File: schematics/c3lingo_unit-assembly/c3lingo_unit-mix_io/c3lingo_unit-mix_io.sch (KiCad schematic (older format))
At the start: 34 parts, among them J3 Stage Line-In, J4 Mix Line-Out, J6 PowerSupply, U3 LM833N, U4 DRV134PA, U5 LM833N

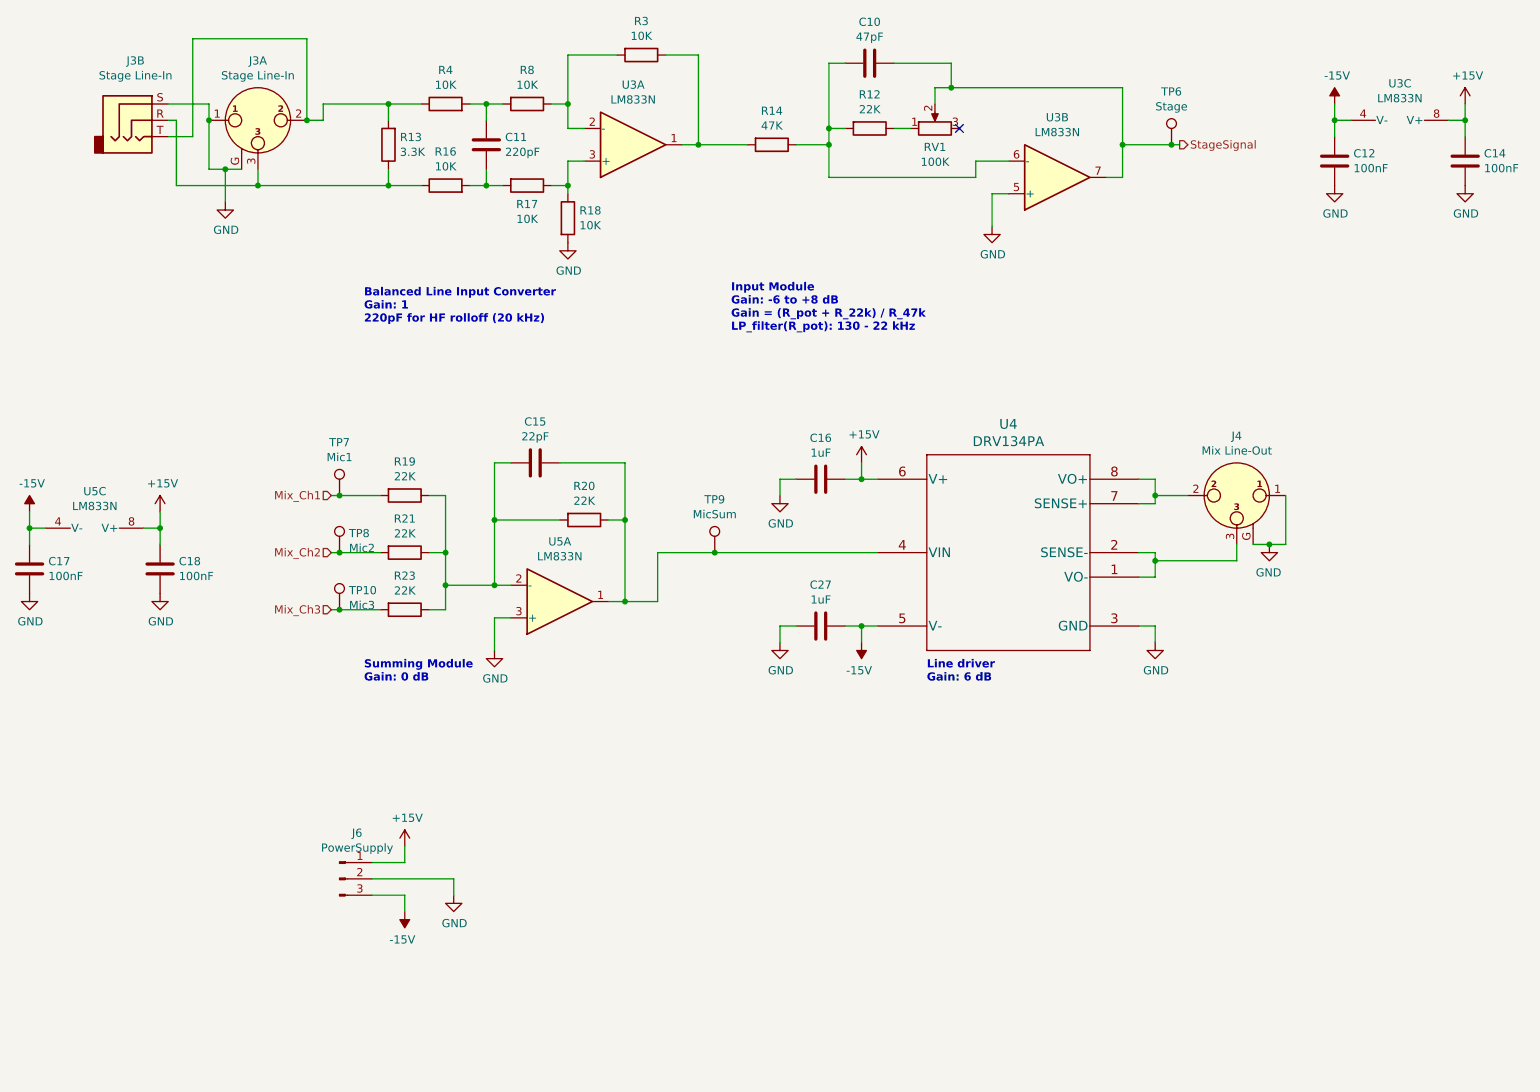
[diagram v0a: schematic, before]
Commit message: [TIDY] Channel Strip: Integrate VU Meter
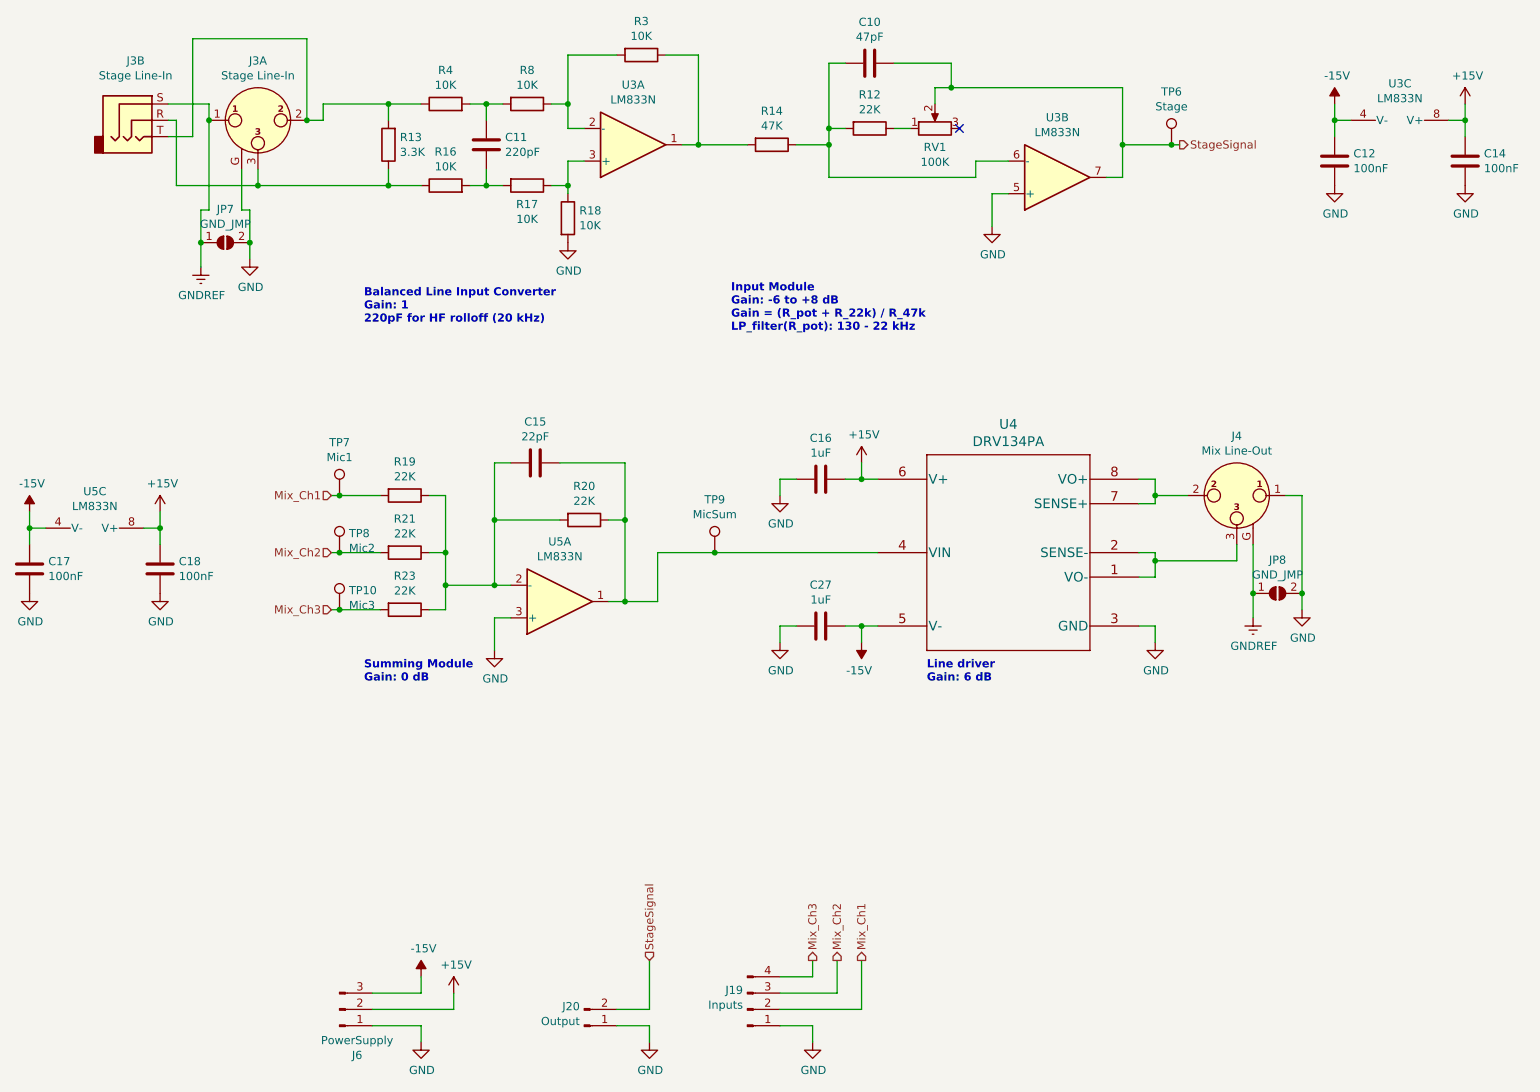
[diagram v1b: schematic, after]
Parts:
- added J19: Inputs, Connector_PinHeader_2.54mm:PinHeader_1x04_P2.54mm_Vertical, symbol Connector:Conn_01x04_Male
- added J20: Output, Connector_PinHeader_2.54mm:PinHeader_1x02_P2.54mm_Vertical, symbol Connector:Conn_01x02_Male
- added JP7, JP8: GND_JMP, Jumper:SolderJumper-2_P1.3mm_Open_TrianglePad1.0x1.5mm, symbol Jumper:SolderJumper_2_Open
- J6: footprint TerminalBlock_MetzConnect:TerminalBlock_MetzConnect_Type073_RT02603HBLU_1x03_P5.08mm_Horizontal -> TerminalBlock_MetzConnect:TerminalBlock_MetzConnect_Type101_RT01603HBWC_1x03_P5.08mm_Horizontal
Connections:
- net +15V: now also J6.2 (Pin_2); no longer J6.1 (Pin_1)
- net GND: now also J6.1 (Pin_1), J19.1 (Pin_1), J20.1 (Pin_1), JP7.2 (B), JP8.2 (B); no longer J3.1, J3.S, J4.G, J6.2 (Pin_2)
- net Mix_Ch1: now also J19.2 (Pin_2)
- net Mix_Ch2: now also J19.3 (Pin_3)
- net Mix_Ch3: now also J19.4 (Pin_4)
- net StageSignal: now also J20.2 (Pin_2)
- new net GNDREF: J3.1, J3.S, J4.G, JP7.1 (A), JP8.1 (A)

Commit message: Schematics: Add missing functionality, add footprints, fix todos
- Add On-Air button
- Lower frequency for the input HPF
- (final) button footprints
- (final) potentiometer values and footprints
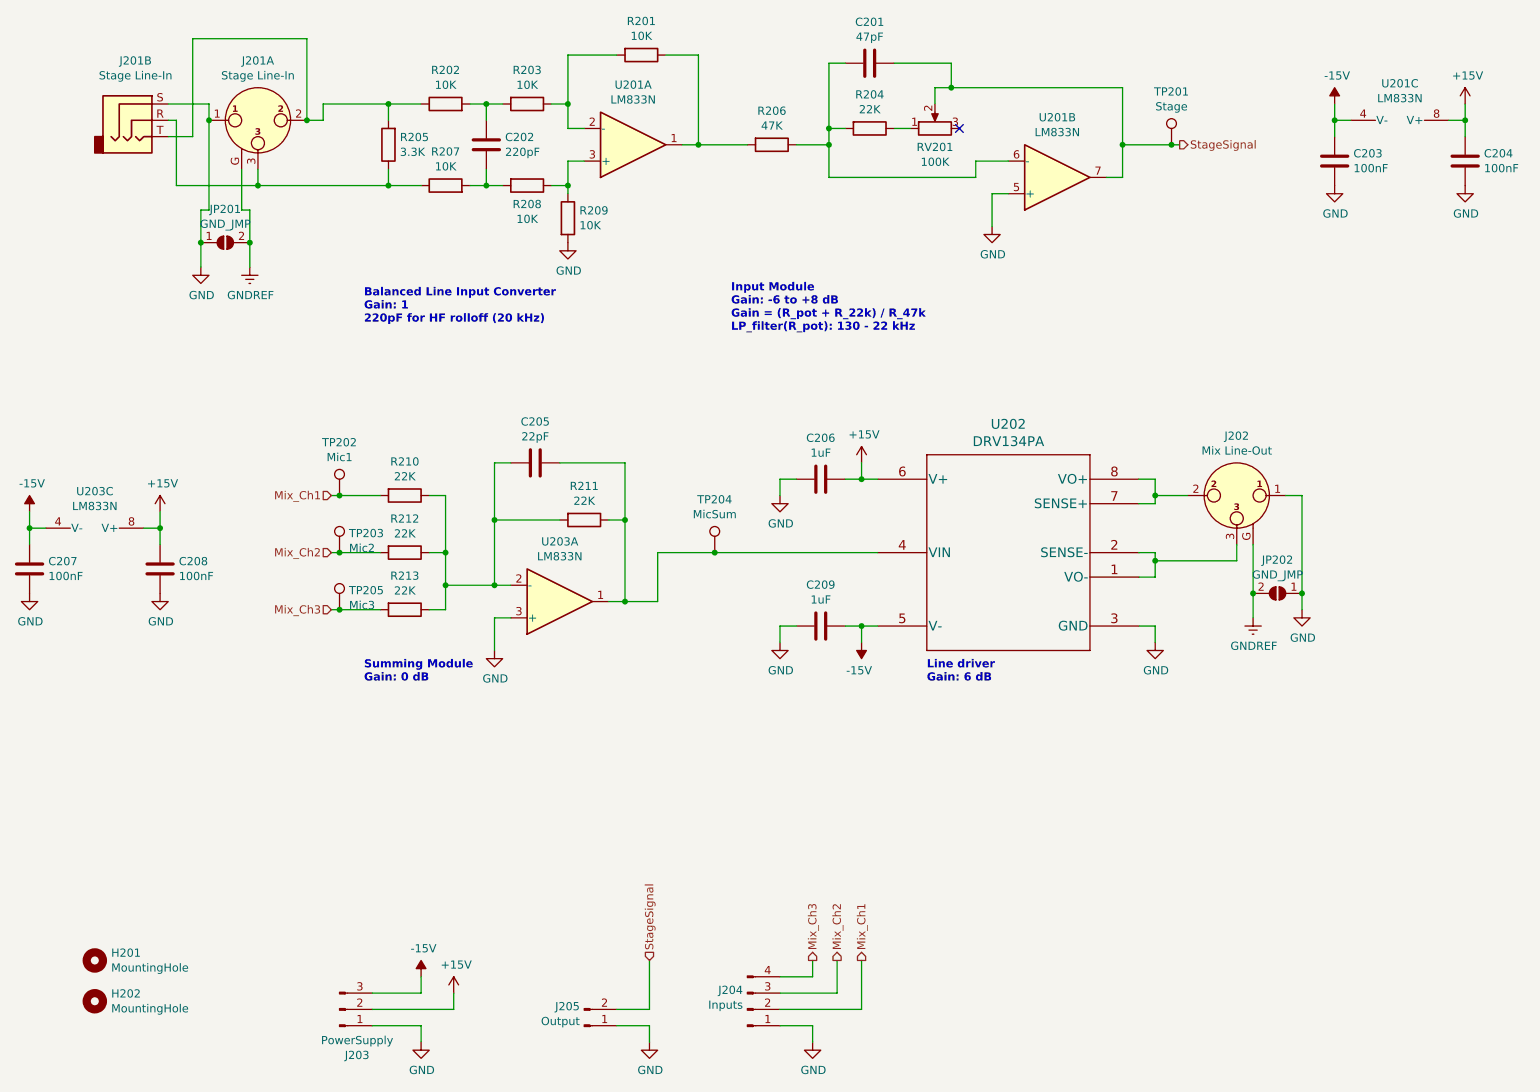
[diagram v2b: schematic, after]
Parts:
- added H201, H202: MountingHole, MountingHole:MountingHole_3.2mm_M3, symbol Mechanical:MountingHole
- J201: renamed from J3; footprint Connector_PinHeader_2.54mm:PinHeader_1x04_P2.54mm_Vertical -> Connector_Audio:Jack_XLR-6.35mm_Neutrik_NCJ6FA-H_Horizontal; Model Combo XLR + 6.3 mm Jack -> NCJ6FA-H (Horiz. Combo Jack)
- J201: renamed from J3; footprint Connector_PinHeader_2.54mm:PinHeader_1x04_P2.54mm_Vertical -> Connector_Audio:Jack_XLR-6.35mm_Neutrik_NCJ6FA-H_Horizontal
- J202: renamed from J4; footprint Connector_PinHeader_2.54mm:PinHeader_1x04_P2.54mm_Vertical -> Connector_Audio:Jack_XLR_Neutrik_NC3MAAH_Horizontal; Model XLR (male) -> NC3MAAH (Horiz. XLR Male)
- J203: renamed from J6; footprint TerminalBlock_MetzConnect:TerminalBlock_MetzConnect_Type101_RT01603HBWC_1x03_P5.08mm_Horizontal -> TerminalBlock_Phoenix:TerminalBlock_Phoenix_PTSM-0,5-3-2.5-H-THR_1x03_P2.50mm_Horizontal
- J204: renamed from J19; footprint Connector_PinHeader_2.54mm:PinHeader_1x04_P2.54mm_Vertical -> TerminalBlock_Phoenix:TerminalBlock_Phoenix_PTSM-0,5-4-2.5-V-THR_1x04_P2.50mm_Vertical; Model TODO: Actual Connector -> PTSM 0,5/ 4-2,5-V THR
- J205: renamed from J20; footprint Connector_PinHeader_2.54mm:PinHeader_1x02_P2.54mm_Vertical -> TerminalBlock_Phoenix:TerminalBlock_Phoenix_PTSM-0,5-2-2.5-V-THR_1x02_P2.50mm_Vertical; Model TODO: Actual Connector -> PTSM 0,5/ 2-2,5-V THR
- RV201: renamed from RV1; Model Vishay M64{Y,Z}104 -> Vishay M64Y104
- renumbered C10 to C201, C11 to C202, C12 to C203, C14 to C204, C15 to C205, C16 to C206, C17 to C207, C18 to C208, C27 to C209, JP7 to JP201, JP8 to JP202, R3 to R201, R4 to R202, R8 to R203, R12 to R204, R13 to R205, R14 to R206, R16 to R207, R17 to R208, R18 to R209, R19 to R210, R20 to R211, R21 to R212, R23 to R213, TP6 to TP201, TP7 to TP202, TP8 to TP203, TP9 to TP204, TP10 to TP205, U3 to U201, U4 to U202, U5 to U203
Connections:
- net GND: now also J201.1, J201.S, JP201.1 (A), JP202.1 (A); no longer J201.G, JP201.2 (B), JP202.2 (B)
- net GNDREF: now also J201.G, JP201.2 (B), JP202.2 (B); no longer J201.1, J201.S, JP201.1 (A), JP202.1 (A)

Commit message: PCB: Line in/out and mics summing design
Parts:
- J203: Model (none) -> PTSM 0,5/ 3-2,5-H THR
- U201, U202, U203: Model (none) -> +DIP-8 Socket
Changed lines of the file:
@@
 F 2 "Package_DIP:DIP-8_W7.62mm_Socket_LongPads" H 4800 2000 50  0001 C CNN
 F 3 "https://www.ti.com/lit/ds/symlink/lm833.pdf" H 4800 2000 50  0001 C CNN
+F 4 "+DIP-8 Socket" H 4800 2000 50  0001 C CNN "Model"
 	1    4800 2000
 	1    0    0    1
@@
 F 2 "Package_DIP:DIP-8_W7.62mm_Socket_LongPads" H 7400 2200 50  0001 C CNN
 F 3 "https://www.ti.com/lit/ds/symlink/lm833.pdf" H 7400 2200 50  0001 C CNN
+F 4 "+DIP-8 Socket" H 7400 2200 50  0001 C CNN "Model"
 	2    7400 2200
 	1    0    0    1
@@
 F 2 "Package_DIP:DIP-8_W7.62mm_Socket_LongPads" H 7100 4540 60  0001 C CNN
 F 3 "https://www.ti.com/lit/ds/symlink/drv134.pdf" H 7100 4581 60  0001 C CNN
+F 4 "+DIP-8 Socket" H 6300 4200 50  0001 C CNN "Model"
 	1    6300 4200
 	1    0    0    -1
@@
 F 2 "Package_DIP:DIP-8_W7.62mm_Socket_LongPads" H 1500 4450 50  0001 C CNN
 F 3 "https://www.ti.com/lit/ds/symlink/lm833.pdf" H 1500 4450 50  0001 C CNN
+F 4 "+DIP-8 Socket" H 1500 4450 50  0001 C CNN "Model"
 	3    1500 4450
 	0    1    1    0
@@
 F 2 "Package_DIP:DIP-8_W7.62mm_Socket_LongPads" H 4350 4800 50  0001 C CNN
 F 3 "https://www.ti.com/lit/ds/symlink/lm833.pdf" H 4350 4800 50  0001 C CNN
+F 4 "+DIP-8 Socket" H 4350 4800 50  0001 C CNN "Model"
 	1    4350 4800
 	1    0    0    1
@@
 F 2 "Package_DIP:DIP-8_W7.62mm_Socket_LongPads" H 9500 1950 50  0001 C CNN
 F 3 "https://www.ti.com/lit/ds/symlink/lm833.pdf" H 9500 1950 50  0001 C CNN
+F 4 "+DIP-8 Socket" H 9500 1950 50  0001 C CNN "Model"
 	3    9500 1950
 	0    1    1    0
@@
 F 2 "TerminalBlock_Phoenix:TerminalBlock_Phoenix_PTSM-0,5-3-2.5-H-THR_1x03_P2.50mm_Horizontal" H 3000 7300 50  0001 C CNN
 F 3 "" H 3000 7300 50  0001 C CNN
+F 4 "PTSM 0,5/ 3-2,5-H THR" H 3000 7300 50  0001 C CNN "Model"
 	1    3000 7300
 	1    0    0    1

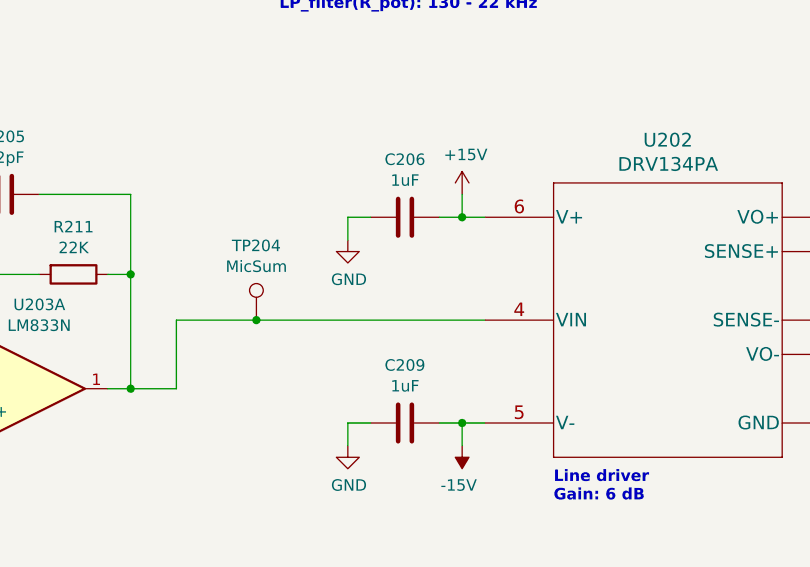
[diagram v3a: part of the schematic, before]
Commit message: [FIX] Schematics: Revised values and PCB errata text
* fixed trim pot range at VU meter
* TODOs removed (5V V_LED didn't work out, 10uF at LM386 wasn't better, VU meter filtering not needed)
* phantom power voltage changed and readme chapter added
* hardware errata: gain pot. pins are swapped, ground plane isn't fully connected

Footprints and PCB aren't fixed to keep the schematic compatible with the existing PCBs!
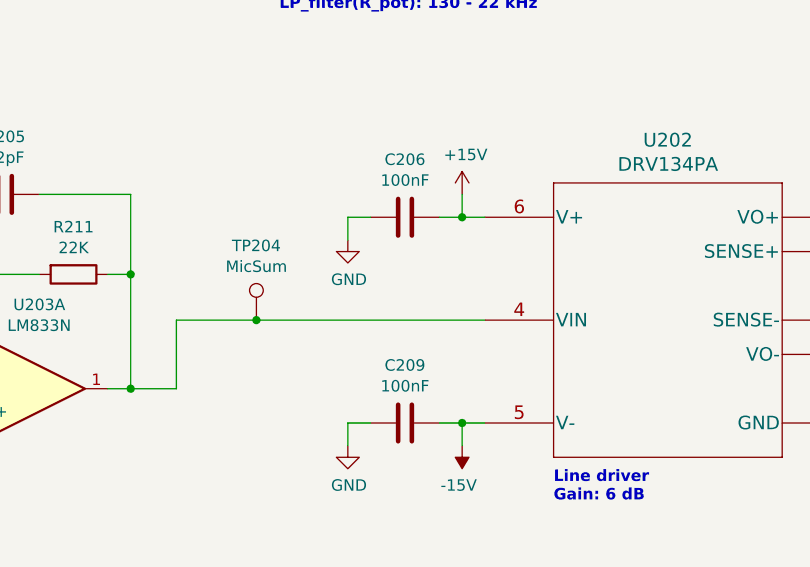
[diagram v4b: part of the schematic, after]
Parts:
- C206, C209: value 1uF -> 100nF
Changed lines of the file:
@@
 Sheet 2 5
 Title "c3lingo interpeter unit -- mix and line I/O"
-Date "2021-05-28"
-Rev "v0.2"
+Date "2021-09-02"
+Rev "v0.2.1"
 Comp "Jannik Beyerstedt (jtbx)"
-Comment1 "Prototype 1"
+Comment1 "Prototype 1 (with errata)"
 Comment2 ""
 Comment3 ""
@@
 P 5950 4050
 F 0 "C206" V 5698 4050 50  0000 C CNN
-F 1 "1uF" V 5789 4050 50  0000 C CNN
+F 1 "100nF" V 5789 4050 50  0000 C CNN
 F 2 "Capacitor_THT:C_Disc_D5.0mm_W2.5mm_P5.00mm" H 5988 3900 50  0001 C CNN
 F 3 "~" H 5950 4050 50  0001 C CNN
@@
 P 5950 4950
 F 0 "C209" V 5698 4950 50  0000 C CNN
-F 1 "1uF" V 5789 4950 50  0000 C CNN
+F 1 "100nF" V 5789 4950 50  0000 C CNN
 F 2 "Capacitor_THT:C_Disc_D5.0mm_W2.5mm_P5.00mm" H 5988 4800 50  0001 C CNN
 F 3 "~" H 5950 4950 50  0001 C CNN
